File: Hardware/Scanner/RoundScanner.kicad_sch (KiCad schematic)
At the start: 2 parts

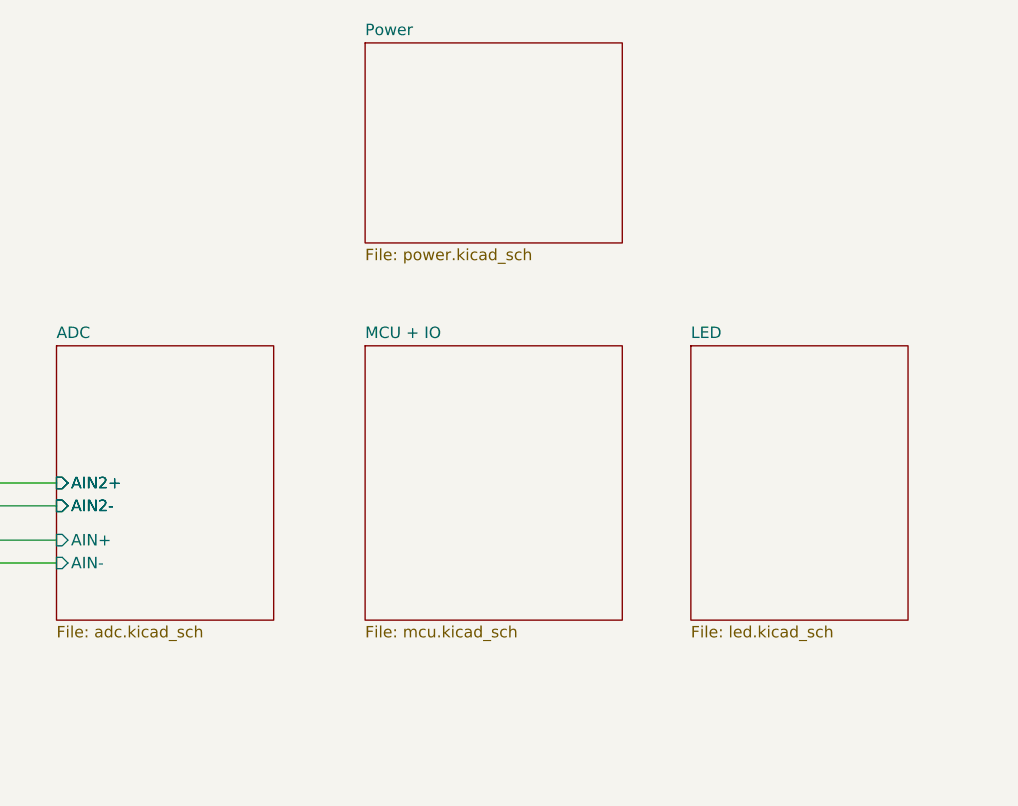
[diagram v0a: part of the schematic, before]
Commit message: added footprint for MTSM2601SMF1-100
Signed-off-by: lokimetasmith <lokimail@gmail.com>
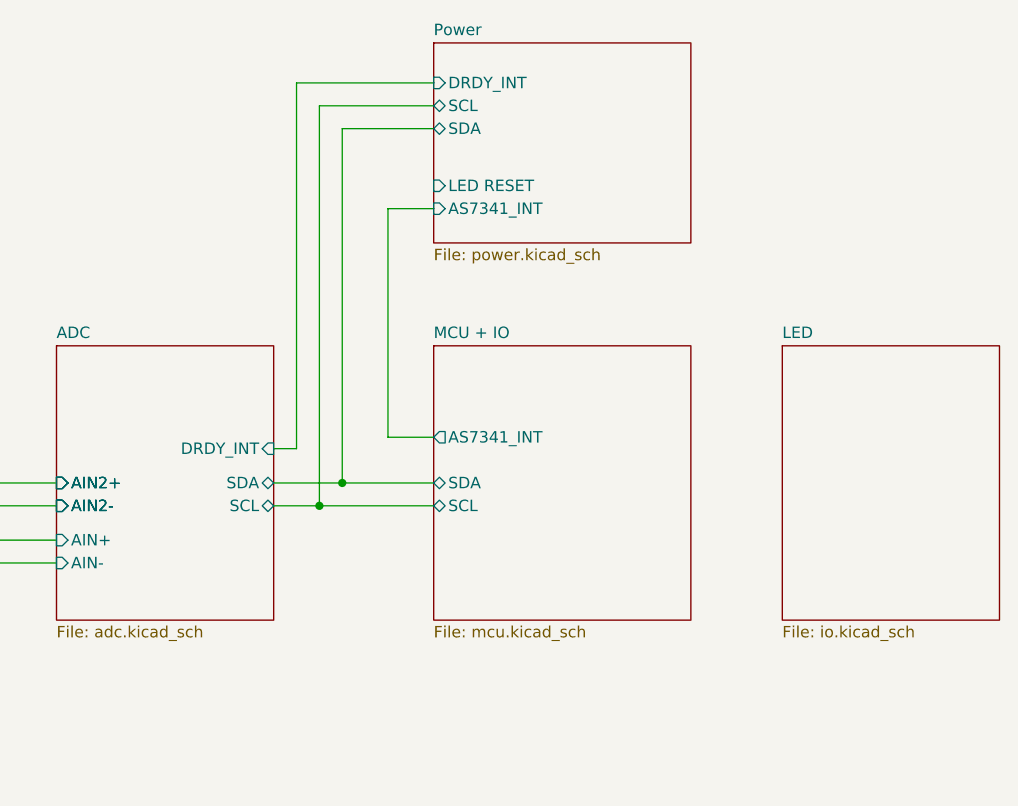
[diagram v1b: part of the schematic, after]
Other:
- sheet ADC ports: added DRDY_INT, SCL, SDA; removed none
- sheet LED: file led.kicad_sch -> io.kicad_sch
- sheet MCU + IO ports: added AS7341_INT, SCL, SDA; removed none
- sheet Power ports: added AS7341_INT, DRDY_INT, LED RESET, SCL, SDA; removed none

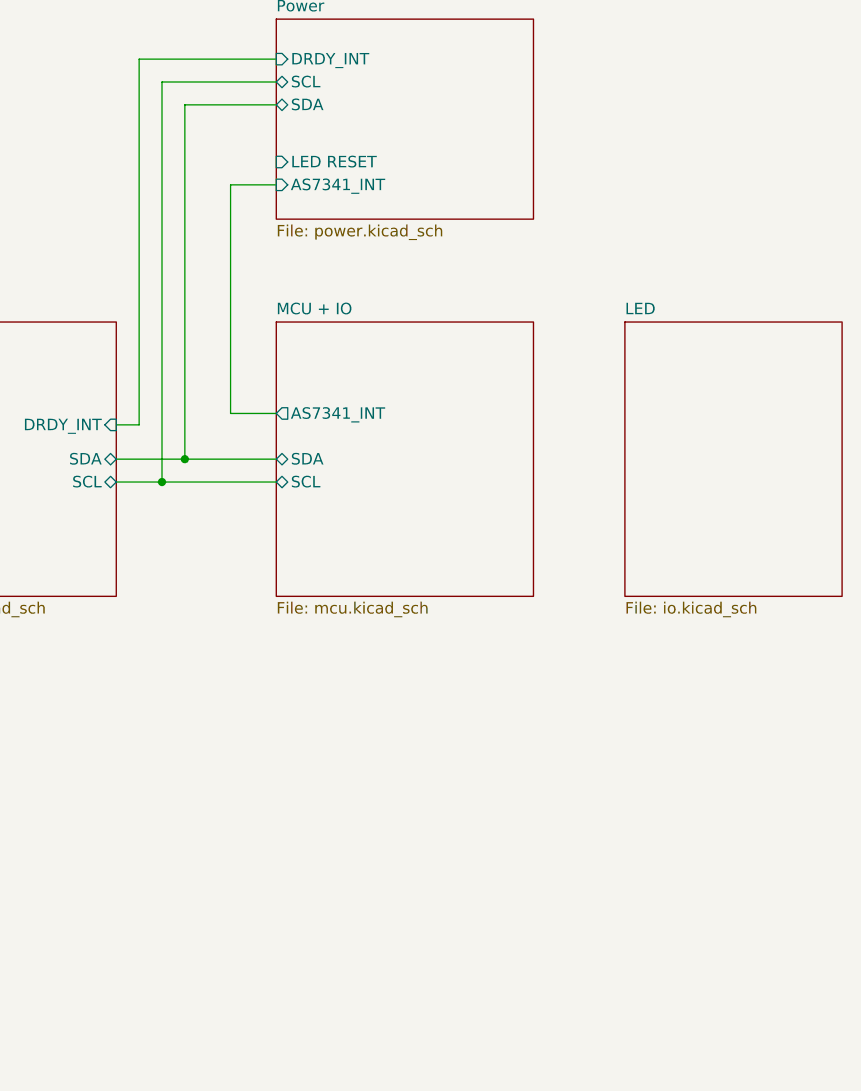
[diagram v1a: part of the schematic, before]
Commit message: lots of changes, added footprints, fixed broken schemaitcs, fixed kicad 7.0 issues
Signed-off-by: lokimetasmith <lokimail@gmail.com>
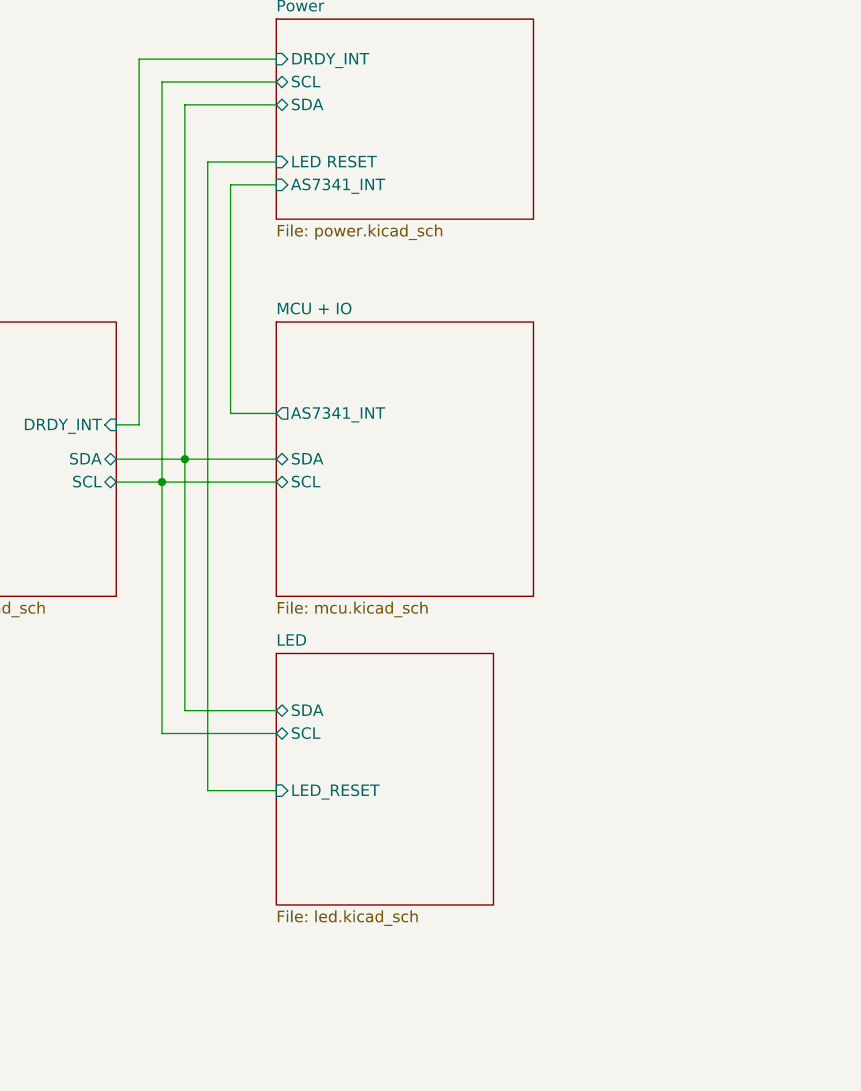
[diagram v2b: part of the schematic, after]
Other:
- sheet LED: file io.kicad_sch -> led.kicad_sch
- sheet LED ports: added LED_RESET, SCL, SDA; removed none
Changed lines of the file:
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@@
   (title_block
     (title "Development Board")
-    (date "2023-10-02")
+    (date "2023-10-29")
     (rev "3")
     (company "Plastic Scanner")
@@
   )
   (junction (at 137.16 92.71) (diameter 0) (color 0 0 0 0)
+  )
+  (wire (pts (xy 139.7 129.54) (xy 139.7 59.69))
+    (stroke (width 0) (type default))
   )
   (wire (pts (xy 147.32 62.23) (xy 142.24 62.23))
@@
     (stroke (width 0) (type default))
   )
+  (wire (pts (xy 147.32 120.65) (xy 137.16 120.65))
+    (stroke (width 0) (type default))
+  )
   (wire (pts (xy 129.54 95.25) (xy 134.62 95.25))
     (stroke (width 0) (type default))
   )
   (wire (pts (xy 129.54 88.9) (xy 132.08 88.9))
+    (stroke (width 0) (type default))
+  )
+  (wire (pts (xy 134.62 123.19) (xy 147.32 123.19))
     (stroke (width 0) (type default))
   )
@@
     (stroke (width 0) (type default))
   )
+  (wire (pts (xy 147.32 129.54) (xy 139.7 129.54))
+    (stroke (width 0) (type default))
+  )
   (wire (pts (xy 92.71 92.71) (xy 105.41 92.71))
+    (stroke (width 0) (type default))
+  )
+  (wire (pts (xy 137.16 120.65) (xy 137.16 92.71))
+    (stroke (width 0) (type default))
+  )
+  (wire (pts (xy 139.7 59.69) (xy 147.32 59.69))
     (stroke (width 0) (type default))
   )
@@
   )
   (wire (pts (xy 134.62 95.25) (xy 147.32 95.25))
+    (stroke (width 0) (type default))
+  )
+  (wire (pts (xy 134.62 95.25) (xy 134.62 123.19))
     (stroke (width 0) (type default))
   )
@@
     )
   )
-  (sheet (at 186.055 77.47) (size 24.13 30.48) (fields_autoplaced)
+  (sheet (at 147.32 114.3) (size 24.13 27.94) (fields_autoplaced)
     (stroke (width 0.1524) (type solid))
     (fill (color 0 0 0 0.0000))
-    (property "Sheetname" "LED" (at 186.055 76.7584 0)
+    (property "Sheetname" "LED" (at 147.32 113.5884 0)
       (effects (font (size 1.27 1.27)) (justify left bottom))
     )
-    (property "Sheetfile" "io.kicad_sch" (at 186.055 108.5346 0)
+    (property "Sheetfile" "led.kicad_sch" (at 147.32 142.8246 0)
       (effects (font (size 1.27 1.27)) (justify left top))
     )
+    (pin "SDA" bidirectional (at 147.32 120.65 180)
+      (effects (font (size 1.27 1.27)) (justify left))
+    )
+    (pin "SCL" bidirectional (at 147.32 123.19 180)
+      (effects (font (size 1.27 1.27)) (justify left))
+    )
+    (pin "LED_RESET" input (at 147.32 129.54 180)
+      (effects (font (size 1.27 1.27)) (justify left))
+    )
     (instances
